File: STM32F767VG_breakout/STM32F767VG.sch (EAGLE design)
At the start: 44 parts, among them IC1 STM32F767VGT6, IC3 LD117AS33TR, X4 8MHz, X5 32.768kHz, X6 MSTBA2

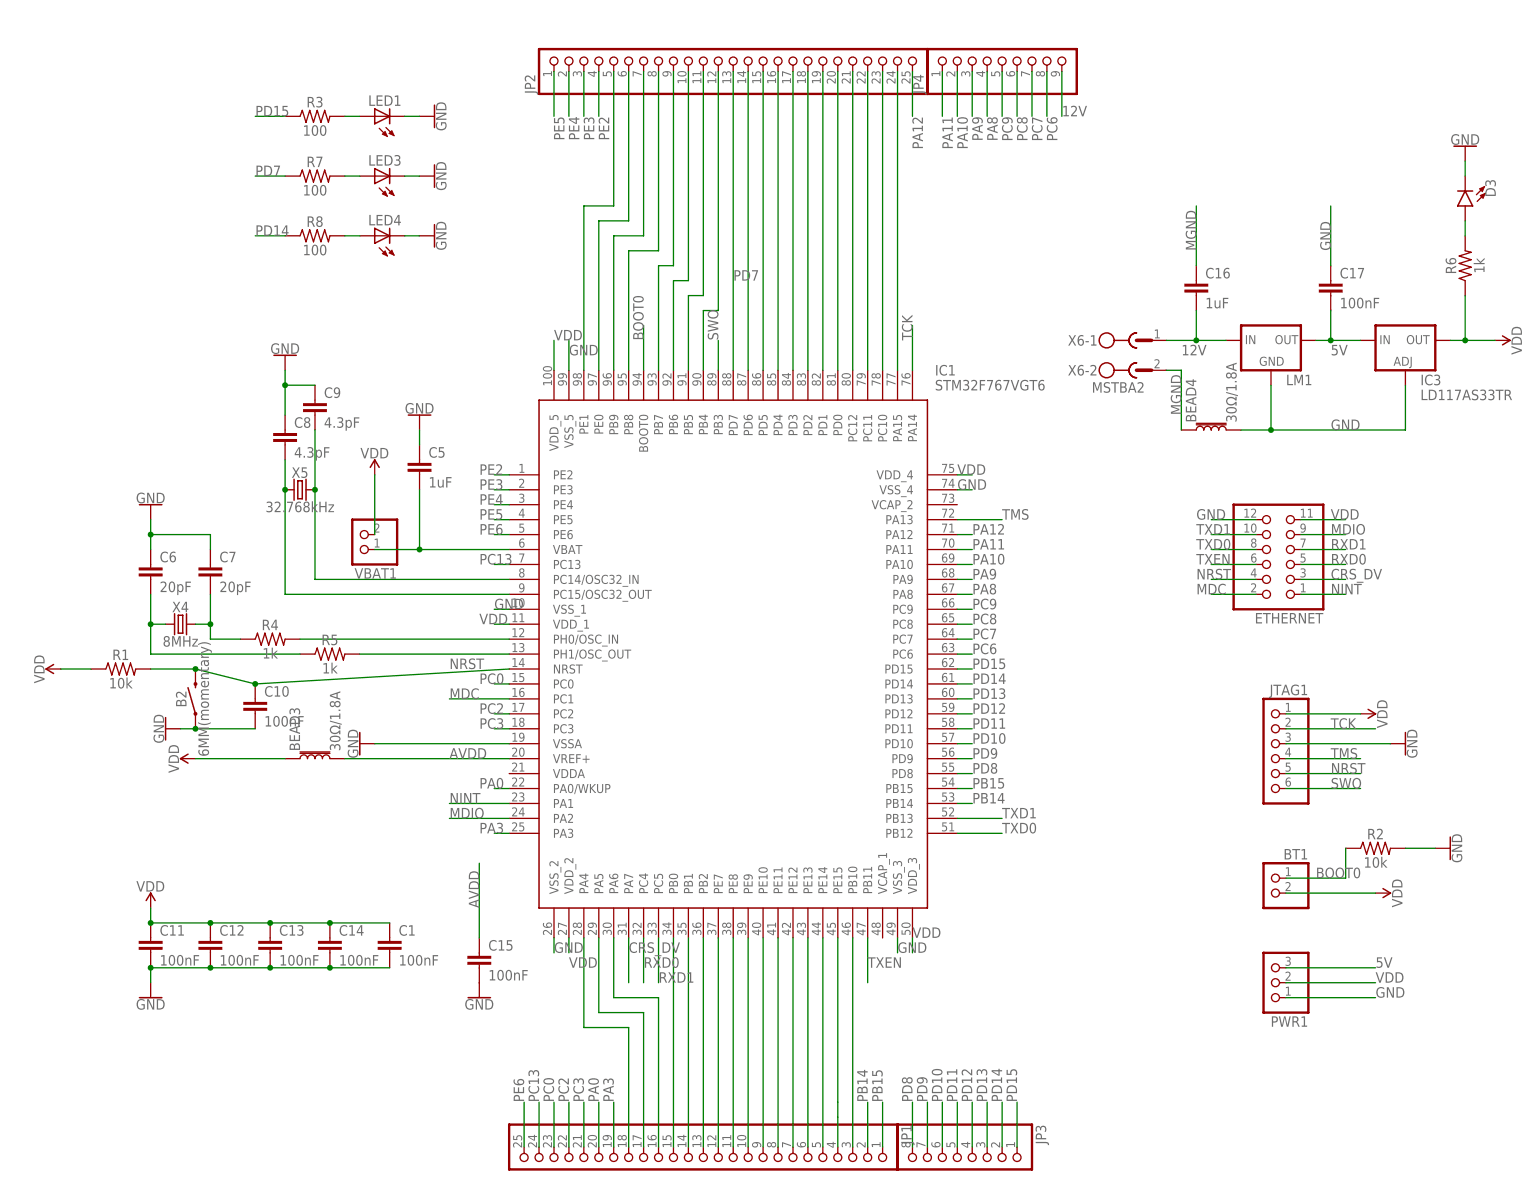
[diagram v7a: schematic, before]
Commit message: Apr 2 Feedback incorporated
Please check if the surface mount of resistors, caps, and LEDs are ok. Also, I noticed there's a lot of free space.
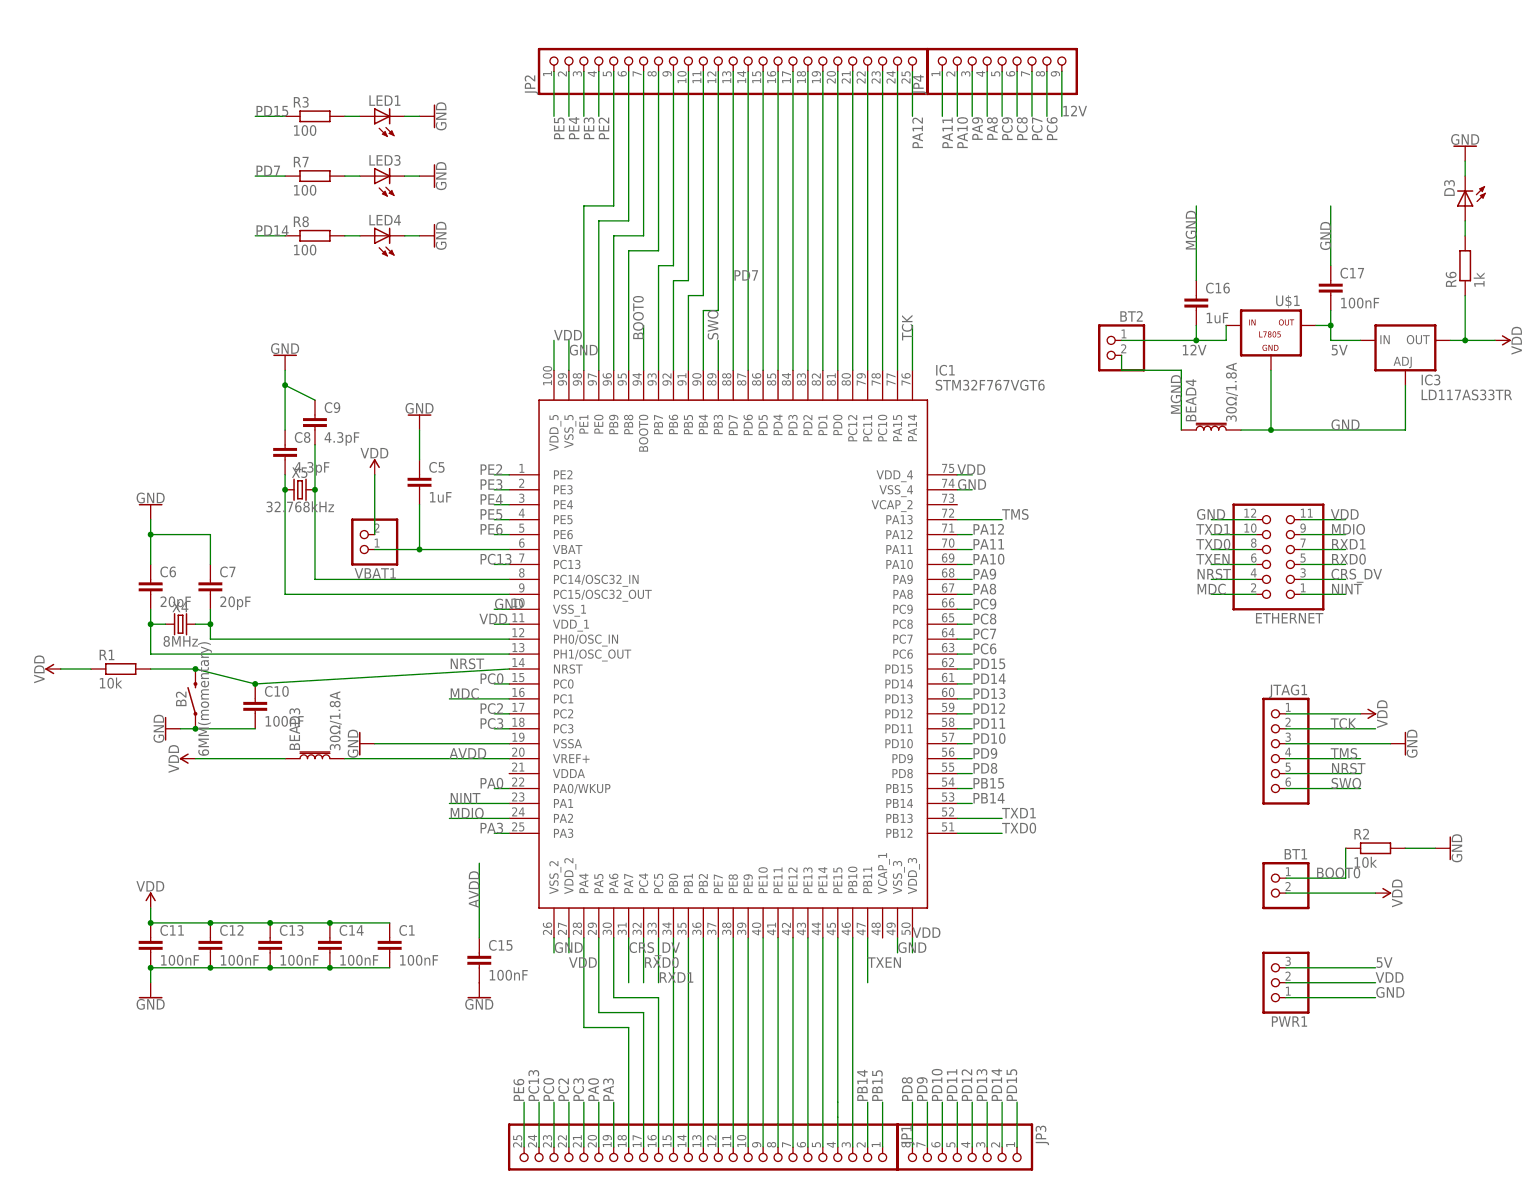
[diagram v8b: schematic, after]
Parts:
- removed LM1: (no value), SparkFun-IC-Power:V_REG_78XX-TO-220
- removed R4, R5: 1k, SparkFun-Resistors:10KOHM-HORIZ-1/4W-1%
- removed X6: MSTBA2, con-phoenix-508:MSTBA2
- added BT2: (no value), pinhead:PINHD-1X2
- added U$1: -L7805, tango:-L7805
- C16, C5: device ee2parts:C5P -> eagle-ltspice:C
- C6, C7, C8, C9: device ee2parts:C2.5P -> eagle-ltspice:C
- D3: device SparkFun-LED:LED5MM -> eagle-ltspice:LED_E
- R1, R2, R3, R7, R8: device SparkFun-Resistors:10KOHM-HORIZ-1/4W-1% -> eagle-ltspice:R
- R6: device SparkFun-Resistors:1KOHM-HORIZ-1/4W-1% -> eagle-ltspice:R
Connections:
- removed net N$16: IC1.PH0/OSC_IN, R4.2
- removed net N$19: IC1.PH1/OSC_OUT, R5.2
- net 12V: now also BT2.1, U$1.IN; no longer LM1.IN, X6-1.1
- net 5V: now also U$1.OUT; no longer LM1.OUT
- net GND: now also U$1.GND; no longer LM1.GND
- net MGND: now also BT2.2; no longer X6-2.1
- net N$21: now also IC1.PH1/OSC_OUT; no longer R5.1
- net N$22: now also IC1.PH0/OSC_IN; no longer R4.1
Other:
- moved on the sheet: C16, C5, C6, C7, C8, C9
